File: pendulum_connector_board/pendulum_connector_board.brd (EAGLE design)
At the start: 9 parts, among them X1 SM07B-SRSS-TB

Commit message: Pendulum control demo in python
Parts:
- added X4: SM02B-SSR-H-TB, con-jst2:SM02B-SSR-H-TB
- moved SERIAL 4.48 mm to (10.3, 12.3)
- moved X1 3.20 mm to (1.92, 12.3)
- moved ENCODER 2.24 mm to (-6.95, 12.3)
- moved PENDULUM 1.44 mm to (-15.3, 12.3)
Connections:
- new net MODE_SWITCH: U$2.P$16, X4.1
- net GND: now also X4.2
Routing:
- net MODE_SWITCH: track 0.00 -> 12.3 mm
- net GND: track 42.9 -> 49.8 mm
- net 3V3: track 41.1 -> 45.2 mm
- net USART_TX: track 31.5 -> 35.4 mm
- net USART_RX: track 31.9 -> 35.3 mm
- net ENC_Z: track 43.4 -> 46.0 mm
- net ENC_B: track 38.2 -> 40.4 mm
- net ENC_A: track 36.3 -> 38.4 mm
- net CS: track 52.9 -> 54.6 mm
- net SER_A: track 19.1 -> 20.7 mm
- net SER_B: track 20.3 -> 21.9 mm
- net SER_Z: track 23.0 -> 24.5 mm
- net SER_Y: track 26.7 -> 28.3 mm
- net TMS: track 22.2 -> 23.6 mm
- net SCK: track 50.2 -> 51.5 mm
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
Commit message: updated boards
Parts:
- added C1, C2, C3: (no value), rcl:E2,5-6
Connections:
- net +24V: now also C1.+, C2.+, C3.+
- net GND: now also C1.-, C2.-, C3.-
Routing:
- net GND: track 49.8 -> 68.1 mm
- net +24V: track 0.00 -> 17.1 mm
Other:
- board text added: "SWITCH"
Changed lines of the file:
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@@
 <text x="-12.48" y="-7.52" size="1" layer="25" font="vector">DC</text>
 <text x="0.48" y="7.36" size="1" layer="25" font="vector">PROG</text>
-<wire x1="23.697159375" y1="-15.83333125" x2="25.437209375" y2="12.852940625" width="0" layer="22" curve="60.555596"/>
-<wire x1="25.437209375" y1="12.852940625" x2="22.759609375" y2="14.499996875" width="0" layer="22" curve="63.193394"/>
-<wire x1="-22.759609375" y1="14.5" x2="22.759609375" y2="14.5" width="0" layer="22"/>
-<wire x1="-22.759609375" y1="14.5" x2="-25.437209375" y2="12.852940625" width="0" layer="22" curve="63.193394"/>
-<wire x1="-25.437209375" y1="12.852940625" x2="-23.697159375" y2="-15.83333125" width="0" layer="22" curve="60.555596"/>
-<wire x1="-23.697159375" y1="-15.83333125" x2="-18.708290625" y2="-18.499996875" width="0" layer="22" curve="56.25096"/>
-<wire x1="-18.708290625" y1="-18.5" x2="18.708290625" y2="-18.5" width="0" layer="22"/>
-<wire x1="18.708290625" y1="-18.5" x2="23.697165625" y2="-15.833334375" width="0" layer="22" curve="56.250995"/>
+<wire x1="23.697159375" y1="-15.83333125" x2="25.437209375" y2="12.852940625" width="0" layer="21" curve="60.555596"/>
+<wire x1="25.437209375" y1="12.852940625" x2="22.759609375" y2="14.499996875" width="0" layer="21" curve="63.193394"/>
+<wire x1="-22.759609375" y1="14.5" x2="22.759609375" y2="14.5" width="0" layer="21"/>
+<wire x1="-22.759609375" y1="14.5" x2="-25.437209375" y2="12.852940625" width="0" layer="21" curve="63.193394"/>
+<wire x1="-25.437209375" y1="12.852940625" x2="-23.697159375" y2="-15.83333125" width="0" layer="21" curve="60.555596"/>
+<wire x1="-23.697159375" y1="-15.83333125" x2="-18.708290625" y2="-18.499996875" width="0" layer="21" curve="56.25096"/>
+<wire x1="-18.708290625" y1="-18.5" x2="18.708290625" y2="-18.5" width="0" layer="21"/>
+<wire x1="18.708290625" y1="-18.5" x2="23.697165625" y2="-15.833334375" width="0" layer="21" curve="56.250995"/>
+<text x="14.24" y="8.64" size="1" layer="25" font="vector">SWITCH</text>
 </plain>
 <attributes>
@@
 <element name="X1" library="con-jst2" package="SM07B-SRSS-TB" value="SM07B-SRSS-TB" x="1.92" y="12.28" smashed="yes" rot="R180"/>
 <element name="X4" library="con-jst2" package="SM02B-SSR-H-TB" value="SM02B-SSR-H-TB" x="16.64" y="12.32" smashed="yes" rot="R180"/>
+<element name="C1" library="rcl" package="E2,5-6" value="" x="-19.36" y="4.64" rot="R90"/>
+<element name="C2" library="rcl" package="E2,5-6" value="" x="-19.36" y="-1.28" rot="R270"/>
+<element name="C3" library="rcl" package="E2,5-6" value="" x="-19.36" y="-7.2" rot="R90"/>
 </elements>
 <signals>
@@
 <wire x1="16.14" y1="10.395" x2="16" y2="10.415" width="0.16" layer="1"/>
 <wire x1="16" y1="10.415" x2="16" y2="6.985" width="0.16" layer="1"/>
-<wire x1="-9.84" y1="-0.47" x2="-9.92" y2="6.56" width="0" layer="19" extent="16-16"/>
+<contactref element="C1" pad="-"/>
+<contactref element="C2" pad="-"/>
+<contactref element="C3" pad="-"/>
+<wire x1="-19.36" y1="5.91" x2="-19.51" y2="5.91" width="1.016" layer="16"/>
+<wire x1="-19.51" y1="5.91" x2="-22.08" y2="8.48" width="1.016" layer="16"/>
+<wire x1="-22.08" y1="8.48" x2="-25.28" y2="8.48" width="1.016" layer="16"/>
+<wire x1="-25.28" y1="8.48" x2="-26.08" y2="7.52" width="1.016" layer="16"/>
+<wire x1="-26.08" y1="7.52" x2="-26.08" y2="-0.46" width="1.016" layer="16"/>
+<wire x1="-26.08" y1="-0.46" x2="-24.635" y2="-1.905" width="1.016" layer="16"/>
+<wire x1="-19.36" y1="5.91" x2="-13.83" y2="7.43" width="0" layer="19" extent="1-1"/>
 </signal>
 <signal name="+24V">
@@
 <vertex x="-25.28" y="7.68"/>
 </polygon>
+<contactref element="C1" pad="+"/>
+<contactref element="C2" pad="+"/>
+<contactref element="C3" pad="+"/>
+<wire x1="-19.36" y1="-8.47" x2="-25.13" y2="-8.47" width="1.016" layer="1"/>
+<wire x1="-25.13" y1="-8.47" x2="-26.08" y2="-7.52" width="1.016" layer="1"/>
+<wire x1="-26.08" y1="-7.52" x2="-26.08" y2="0.46" width="1.016" layer="1"/>
+<wire x1="-26.08" y1="0.46" x2="-24.635" y2="1.905" width="1.016" layer="1"/>
 </signal>
 <signal name="PHASA">

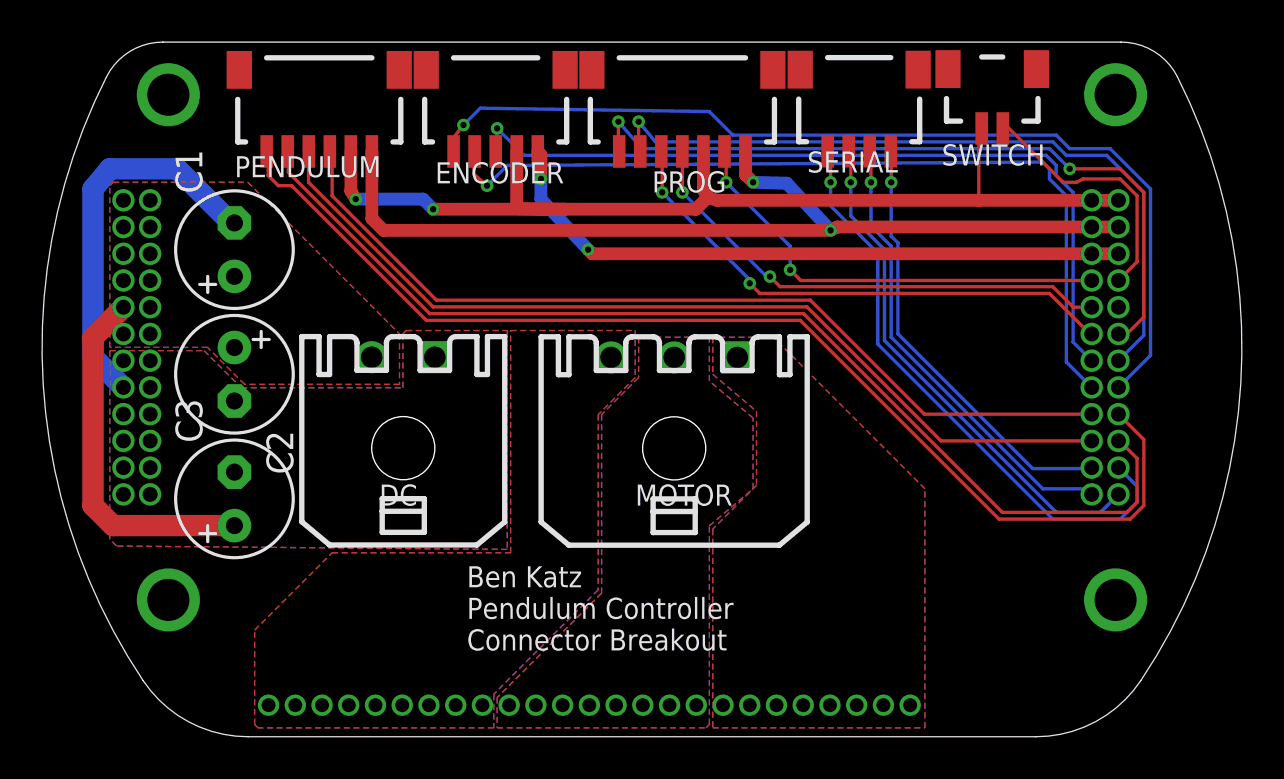
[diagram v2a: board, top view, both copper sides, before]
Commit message: updated pendulum software
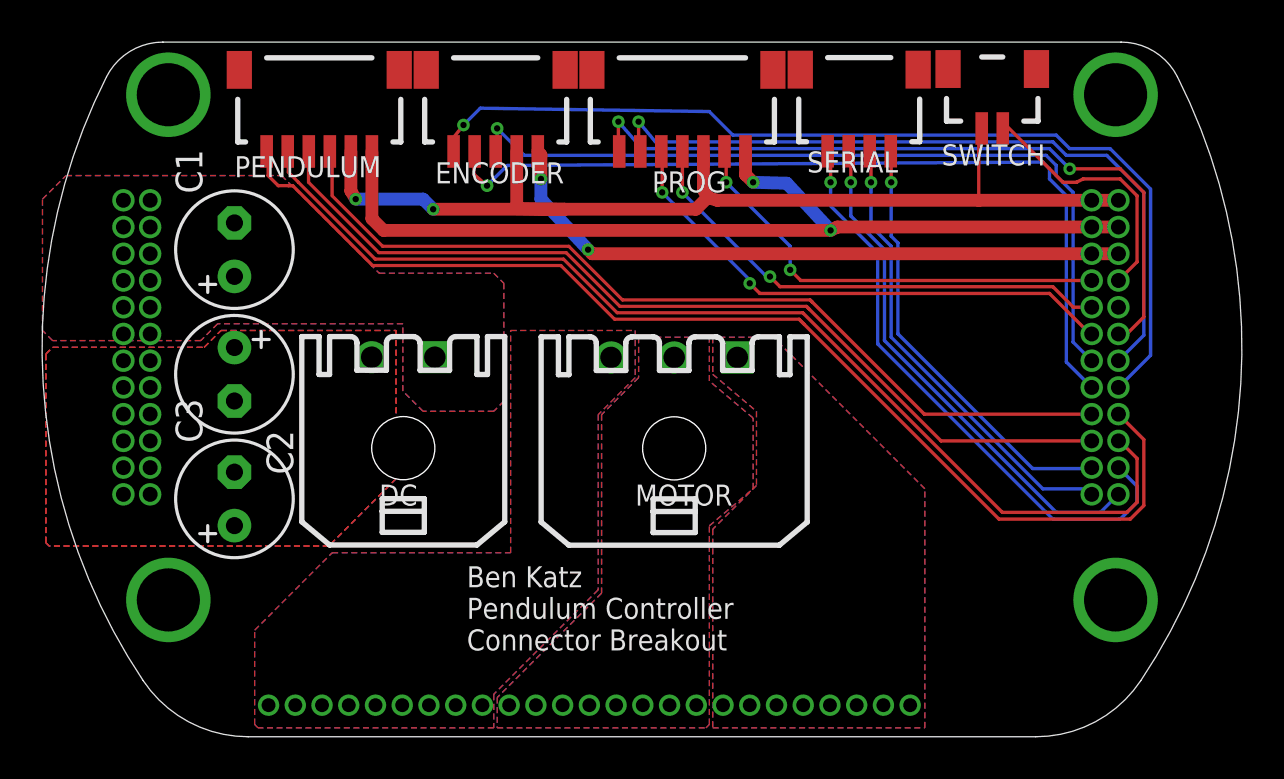
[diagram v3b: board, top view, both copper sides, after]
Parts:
- turned U$5 to 180 degrees
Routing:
- net GND: track 68.1 -> 50.0 mm
- net +24V: track 17.1 -> 0.00 mm

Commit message: fixing controller BOM mistake
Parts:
- removed C3: (no value), rcl:E2,5-6
- moved C2 0.96 mm to (-19.4, -2.24), turned to 90 degrees
- moved DC 0.48 mm to (-10.9, -4.79)
- moved C1 0.36 mm to (-19.2, 4.32)
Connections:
- net +24V: no longer C3.+
- net GND: no longer C3.-
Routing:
- removed copper zone on layer 16, net +24V
- removed copper zone on layer 1, net GND
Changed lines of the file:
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@@
 <?xml version="1.0" encoding="utf-8"?>
 <!DOCTYPE eagle SYSTEM "eagle.dtd">
-<eagle version="9.4.2">
+<eagle version="9.6.2">
 <drawing>
 <settings>
@@
 Pendulum Controller
 Connector Breakout</text>
-<text x="-0.32" y="-7.52" size="1" layer="25" font="vector">MOTOR</text>
-<text x="-12.48" y="-7.52" size="1" layer="25" font="vector">DC</text>
-<text x="0.48" y="7.36" size="1" layer="25" font="vector">PROG</text>
+<text x="-0.64" y="1.28" size="1" layer="25" font="vector">MOTOR</text>
+<text x="-12.64" y="1.44" size="1" layer="25" font="vector">DC</text>
+<text x="0" y="8.32" size="1" layer="25" font="vector">PROG</text>
 <wire x1="23.697159375" y1="-15.83333125" x2="25.437209375" y2="12.852940625" width="0" layer="21" curve="60.555596"/>
 <wire x1="25.437209375" y1="12.852940625" x2="22.759609375" y2="14.499996875" width="0" layer="21" curve="63.193394"/>
@@
 <wire x1="-18.708290625" y1="-18.5" x2="18.708290625" y2="-18.5" width="0" layer="21"/>
 <wire x1="18.708290625" y1="-18.5" x2="23.697165625" y2="-15.833334375" width="0" layer="21" curve="56.250995"/>
-<text x="14.24" y="8.64" size="1" layer="25" font="vector">SWITCH</text>
+<text x="14.4" y="8.96" size="1" layer="25" font="vector">SWITCH</text>
 </plain>
 <attributes>
@@
 <elements>
 <element name="MOTOR" library="con-molex-micro-fit-3_0" package="43650-0300" value="" x="1.53" y="-4.8" smashed="yes"/>
-<element name="DC" library="con-molex-micro-fit-3_0" package="43650-0200" value="" x="-11.34" y="-4.79" smashed="yes"/>
+<element name="DC" library="con-molex-micro-fit-3_0" package="43650-0200" value="" x="-10.86" y="-4.79" smashed="yes"/>
 <element name="SERIAL" library="con-jst2" package="SM04B-SRSS-TB" value="SM04B-SRSS-TB" x="10.32" y="12.29" smashed="yes" rot="R180">
-<attribute name="NAME" x="7.845" y="8.305" size="1" layer="25" font="vector"/>
+<attribute name="NAME" x="7.725" y="8.365" size="1" layer="25" font="vector"/>
 </element>
 <element name="ENCODER" library="con-jst2" package="SM05B-SRSS-TB" value="SM05B-SRSS-TB" x="-6.95" y="12.28" smashed="yes" rot="R180">
-<attribute name="NAME" x="-9.825" y="7.79" size="1" layer="25" font="vector"/>
+<attribute name="NAME" x="-9.865" y="8.21" size="1" layer="25" font="vector"/>
 </element>
 <element name="PENDULUM" library="con-jst2" package="SM06B-SRSS-TB" value="SM06B-SRSS-TB" x="-15.33" y="12.28" smashed="yes" rot="R180">
-<attribute name="NAME" x="-19.355" y="8.08" size="1" layer="25" font="vector"/>
+<attribute name="NAME" x="-18.825" y="7.99" size="1" layer="25" font="vector"/>
 </element>
 <element name="U$5" library="Ben_Library" package="2X12X.05" value="HEADER_2X12" x="-24" y="0" smashed="yes" rot="R180"/>
 <element name="U$4" library="Ben_Library" package="1X25X.05" value="HEADER_1X25" x="-2.5" y="-17" smashed="yes" rot="R90"/>
 <element name="U$2" library="Ben_Library" package="2X12X.05" value="HEADER_2X12" x="22" y="0" smashed="yes"/>
-<element name="X1" library="con-jst2" package="SM07B-SRSS-TB" value="SM07B-SRSS-TB" x="1.92" y="12.28" smashed="yes" rot="R180"/>
-<element name="X4" library="con-jst2" package="SM02B-SSR-H-TB" value="SM02B-SSR-H-TB" x="16.64" y="12.32" smashed="yes" rot="R180"/>
-<element name="C1" library="rcl" package="E2,5-6" value="" x="-19.36" y="4.64" smashed="yes" rot="R90">
-<attribute name="NAME" x="-20.884" y="7.307" size="1.27" layer="25" ratio="10" rot="R90"/>
-<attribute name="VALUE" x="-16.693" y="7.307" size="1.27" layer="27" ratio="10" rot="R90"/>
+<element name="X1" library="con-jst2" package="SM07B-SRSS-TB" value="SM07B-SRSS-TB" x="1.92" y="12.28" smashed="yes" rot="R180">
+<attribute name="NAME" x="0.535" y="11.315" size="1" layer="25" font="vector"/>
 </element>
-<element name="C2" library="rcl" package="E2,5-6" value="" x="-19.36" y="-1.28" smashed="yes" rot="R270">
-<attribute name="NAME" x="-17.836" y="-3.947" size="1.27" layer="25" ratio="10" rot="R270"/>
-<attribute name="VALUE" x="-22.027" y="-3.947" size="1.27" layer="27" ratio="10" rot="R270"/>
+<element name="X4" library="con-jst2" package="SM02B-SSR-H-TB" value="SM02B-SSR-H-TB" x="16.64" y="12.32" smashed="yes" rot="R180">
+<attribute name="NAME" x="15.855" y="11.65" size="1" layer="25" font="vector"/>
 </element>
-<element name="C3" library="rcl" package="E2,5-6" value="" x="-19.36" y="-7.2" smashed="yes" rot="R90">
-<attribute name="NAME" x="-20.884" y="-4.533" size="1.27" layer="25" ratio="10" rot="R90"/>
-<attribute name="VALUE" x="-16.693" y="-4.533" size="1.27" layer="27" ratio="10" rot="R90"/>
+<element name="C1" library="rcl" library_urn="urn:adsk.eagle:library:334" package="E2,5-6" package3d_urn="urn:adsk.eagle:package:23349/1" value="" x="-19.2" y="4.32" smashed="yes" rot="R90">
+<attribute name="NAME" x="-16.267" y="1.996" size="0.5" layer="25" font="vector" ratio="10" rot="R180"/>
+<attribute name="POPULARITY" value="14" x="-19.2" y="4.32" size="1.778" layer="27" rot="R90" display="off"/>
+<attribute name="SPICEPREFIX" value="C" x="-19.2" y="4.32" size="1.778" layer="27" rot="R90" display="off"/>
+<attribute name="VALUE" x="-16.533" y="6.987" size="1.27" layer="27" ratio="10" rot="R90"/>
+</element>
+<element name="C2" library="rcl" library_urn="urn:adsk.eagle:library:334" package="E2,5-6" package3d_urn="urn:adsk.eagle:package:23349/1" value="" x="-19.36" y="-2.24" smashed="yes" rot="R90">
+<attribute name="NAME" x="-21.547" y="6.316" size="0.5" layer="25" font="vector" ratio="10" rot="R180"/>
+<attribute name="POPULARITY" value="14" x="-19.36" y="-2.24" size="1.778" layer="27" rot="R90" display="off"/>
+<attribute name="SPICEPREFIX" value="C" x="-19.36" y="-2.24" size="1.778" layer="27" rot="R90" display="off"/>
+<attribute name="VALUE" x="-16.693" y="0.427" size="1.27" layer="27" ratio="10" rot="R90"/>
 </element>
 </elements>
@@
 <contactref element="C1" pad="-"/>
 <contactref element="C2" pad="-"/>
-<contactref element="C3" pad="-"/>
-<wire x1="-19.36" y1="5.91" x2="-19.51" y2="5.91" width="1.016" layer="16"/>
-<polygon width="0.1524" layer="1" isolate="0.25" thermals="no" rank="2">
-<vertex x="-11.36" y="-2.08"/>
-<vertex x="-11.36" y="1.12"/>
-<vertex x="-20.16" y="1.12"/>
-<vertex x="-20.96" y="0.32"/>
-<vertex x="-28" y="0.32"/>
-<vertex x="-28.48" y="0.8"/>
-<vertex x="-28.48" y="7.04"/>
-<vertex x="-27.36" y="8.16"/>
-<vertex x="-17.12" y="8.16"/>
-<vertex x="-12.48" y="3.52"/>
-<vertex x="-7.04" y="3.52"/>
-<vertex x="-6.56" y="3.04"/>
-<vertex x="-6.56" y="-2.56"/>
-<vertex x="-7.04" y="-3.04"/>
-<vertex x="-10.4" y="-3.04"/>
+<polygon width="0.1524" layer="16" thermals="no">
+<vertex x="-6.72" y="3.2"/>
+<vertex x="-13.92" y="3.2"/>
+<vertex x="-18.88" y="8.16"/>
+<vertex x="-26.72" y="8.16"/>
+<vertex x="-26.72" y="-9.28"/>
+<vertex x="-6.72" y="-9.28"/>
 </polygon>
-<polygon width="0.1524" layer="16" isolate="0.25" thermals="no" rank="2">
-<vertex x="-11.36" y="-2.08"/>
-<vertex x="-11.36" y="1.12"/>
-<vertex x="-20.16" y="1.12"/>
-<vertex x="-20.96" y="0.32"/>
-<vertex x="-28" y="0.32"/>
-<vertex x="-28.48" y="0.8"/>
-<vertex x="-28.48" y="7.04"/>
-<vertex x="-27.36" y="8.16"/>
-<vertex x="-17.12" y="8.16"/>
-<vertex x="-12.48" y="3.52"/>
-<vertex x="-7.04" y="3.52"/>
-<vertex x="-6.56" y="3.04"/>
-<vertex x="-6.56" y="-2.56"/>
-<vertex x="-7.04" y="-3.04"/>
-<vertex x="-10.4" y="-3.04"/>
-</polygon>
-<wire x1="-19.36" y1="-2.55" x2="-19.36" y2="-5.93" width="0" layer="19" extent="1-1"/>
-<wire x1="-23.365" y1="0.635" x2="-19.36" y2="-2.55" width="0" layer="19" extent="1-1"/>
-<wire x1="-13.83" y1="7.43" x2="-19.36" y2="5.91" width="0" layer="19" extent="1-1"/>
+<wire x1="-19.2" y1="5.59" x2="-13.6" y2="7.04" width="0" layer="19" extent="1-1"/>
 </signal>
 <signal name="+24V">
@@
 <contactref element="C1" pad="+"/>
 <contactref element="C2" pad="+"/>
-<contactref element="C3" pad="+"/>
-<polygon width="0.1524" layer="1" isolate="0.25" thermals="no">
-<vertex x="-28" y="0"/>
-<vertex x="-20.8" y="0"/>
-<vertex x="-20" y="0.8"/>
-<vertex x="-11.68" y="0.8"/>
-<vertex x="-11.68" y="-6.24"/>
-<vertex x="-14.88" y="-9.44"/>
-<vertex x="-28.16" y="-9.44"/>
-<vertex x="-28.32" y="-9.28"/>
-<vertex x="-28.32" y="-0.32"/>
+<polygon width="0.1524" layer="1" thermals="no" rank="2">
+<vertex x="-6.88" y="3.2"/>
+<vertex x="-13.92" y="3.2"/>
+<vertex x="-18.88" y="8.16"/>
+<vertex x="-26.72" y="8.16"/>
+<vertex x="-26.72" y="-9.28"/>
+<vertex x="-6.72" y="-9.28"/>
+<vertex x="-6.72" y="3.04"/>
 </polygon>
-<polygon width="0.1524" layer="16" isolate="0.25" thermals="no">
-<vertex x="-28" y="0"/>
-<vertex x="-20.8" y="0"/>
-<vertex x="-20" y="0.8"/>
-<vertex x="-11.68" y="0.8"/>
-<vertex x="-11.68" y="-6.24"/>
-<vertex x="-14.88" y="-9.44"/>
-<vertex x="-28.16" y="-9.44"/>
-<vertex x="-28.32" y="-9.28"/>
-<vertex x="-28.32" y="-0.32"/>
-</polygon>
-<polygon width="0.1524" layer="1" isolate="0.25" thermals="no">
-<vertex x="-28" y="0"/>
-<vertex x="-20.8" y="0"/>
-<vertex x="-20" y="0.8"/>
-<vertex x="-11.68" y="0.8"/>
-<vertex x="-11.68" y="-6.24"/>
-<vertex x="-14.88" y="-9.44"/>
-<vertex x="-28.16" y="-9.44"/>
-<vertex x="-28.32" y="-9.28"/>
-<vertex x="-28.32" y="-0.32"/>
-</polygon>
-<wire x1="-19.36" y1="-0.01" x2="-19.36" y2="3.37" width="0" layer="19" extent="1-1"/>
 </signal>
 <signal name="PHASA">
@@
 which will not be processed correctly with this version.
 </note>
+<note version="8.2" severity="warning">
+Since Version 8.2, EAGLE supports online libraries. The ids
+of those online libraries will not be understood (or retained)
+with this version.
+</note>
+<note version="8.3" severity="warning">
+Since Version 8.3, EAGLE supports URNs for individual library
+assets (packages, symbols, and devices). The URNs of those assets
+will not be understood (or retained) with this version.
+</note>
+<note version="8.3" severity="warning">
+Since Version 8.3, EAGLE supports the association of 3D packages
+with devices in libraries, schematics, and board files. Those 3D
+packages will not be understood (or retained) with this version.
+</note>
 </compatibility>
